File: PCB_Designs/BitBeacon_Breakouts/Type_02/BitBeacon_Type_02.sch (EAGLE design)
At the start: 100 parts, among them IC1 AD8603UJ, IC2 AD8603UJ, IC3 AD8603UJ, IC4 AD8603UJ

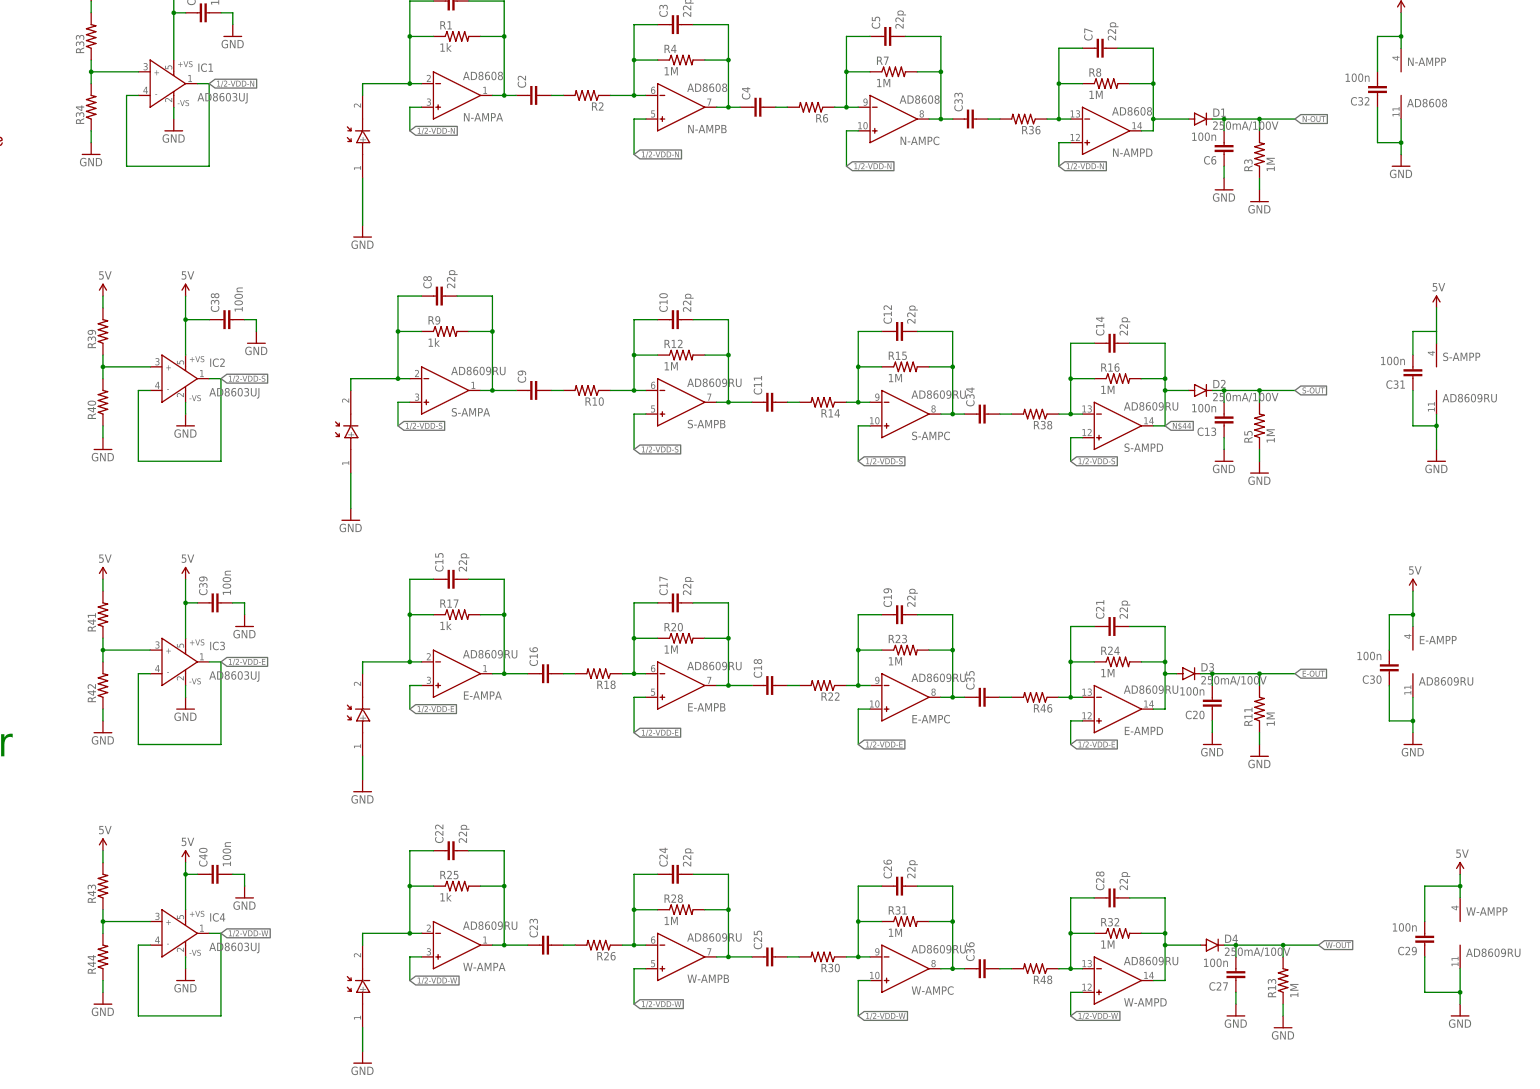
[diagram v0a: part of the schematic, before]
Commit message: updates to code to include Bluetooth, updates to BitBeacon circuit to include labels, indicator LEDs, added BitBeacon Breakout to prototype different signal amplifier types
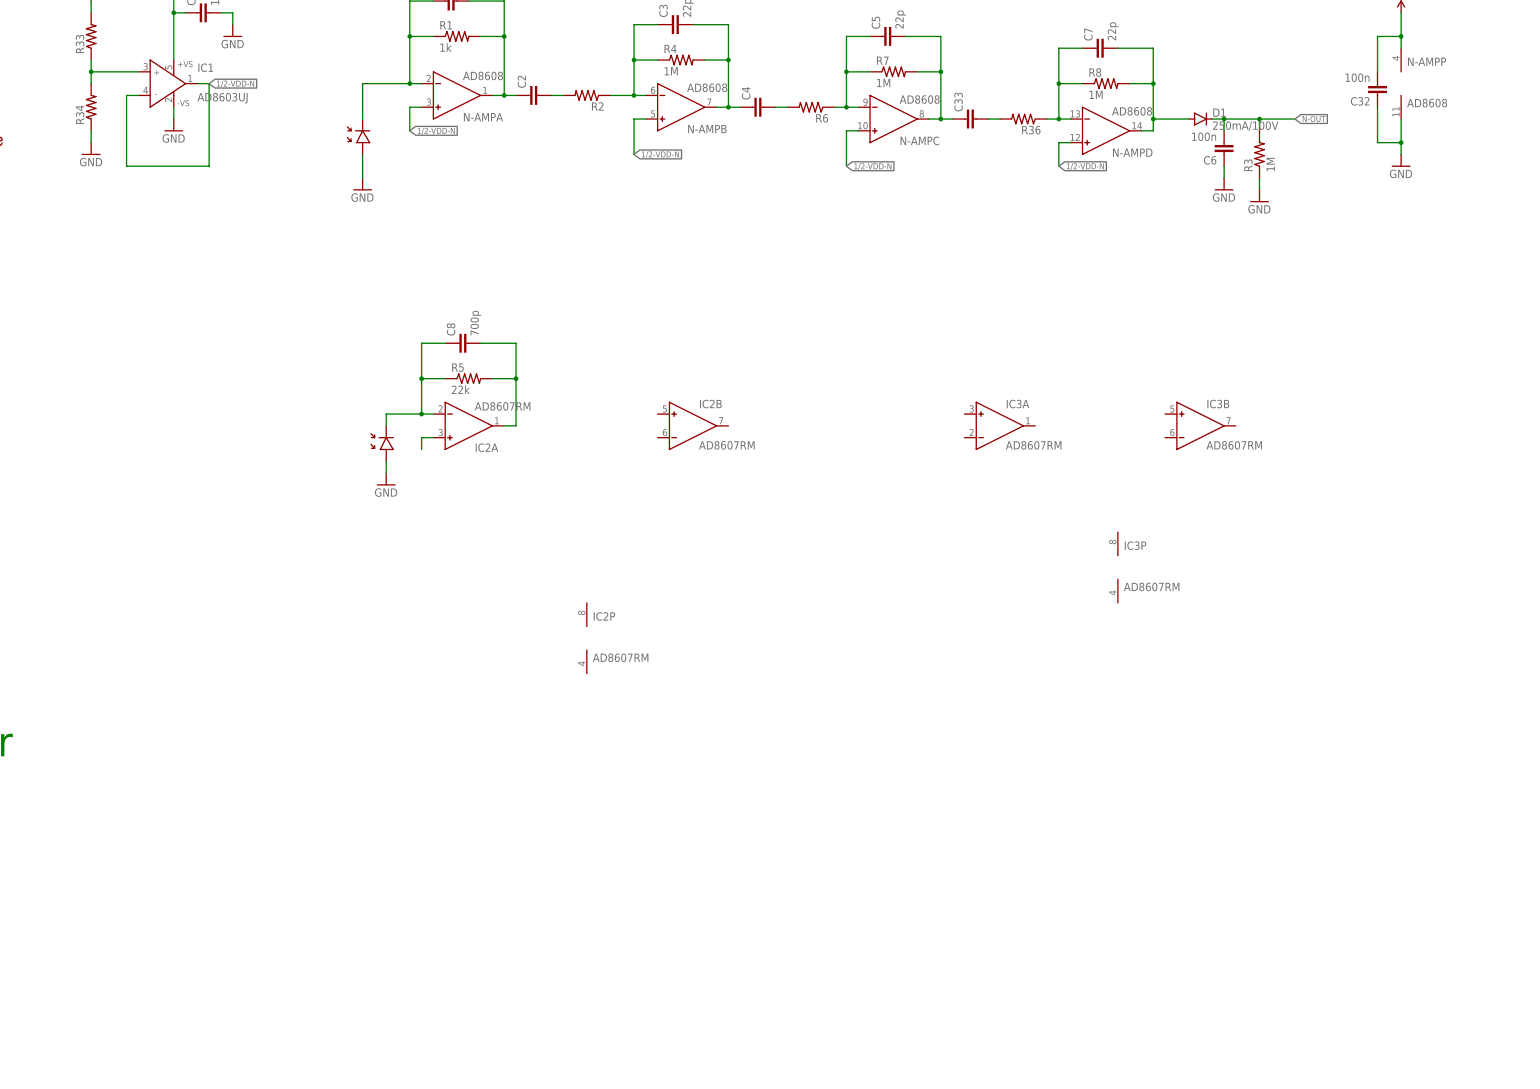
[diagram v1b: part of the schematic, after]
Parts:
- removed C10, C12, C14, C15, C17, C19, C21, C22, C24, C26, C28: 22p, resistor:C-EUC0402
- removed C11, C16, C18, C23, C25, C34, C35, C36, C9: (no value), resistor:C-EUC0402
- removed C13, C20, C27, C29, C30, C31, C38, C39, C40: 100n, resistor:C-EUC0402
- removed D2, D3, D4: 250mA/100V, SparkFun-DiscreteSemi:DIODEBAS16
- removed E-AMP, S-AMP, W-AMP: AD8609RU, analog-devices:AD8609RU
- removed E-PD1, S-PD1, W-PD1: BPW46, Orlando:BPW46
- removed IC4: AD8603UJ, analog-devices:AD8603UJ
- removed R10, R14, R18, R22, R26, R30, R38, R39, R40, R41, R42, R43, R44, R46, R48: (no value), resistor:R-US_R0402
- removed R11, R12, R13, R15, R16, R20, R23, R24, R28, R31, R32: 1M, resistor:R-US_R0402
- removed R17, R25, R9: 1k, resistor:R-US_R0402
- added N-PD2: BPW46, Orlando:BPW46
- C8: value 22p -> 700p
- IC2, IC3: value AD8603UJ -> AD8607RM; device analog-devices:AD8603UJ -> analog-devices:AD8607RM
- R5: value 1M -> 22k
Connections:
- removed net 1/2-VDD-E: E-AMPA.IN+, E-AMPB.IN+, E-AMPC.IN+, E-AMPD.IN+, IC3.IN-, IC3.OUT
- removed net 1/2-VDD-S: IC2.IN-, IC2.OUT, S-AMPA.IN+, S-AMPB.IN+, S-AMPC.IN+, S-AMPD.IN+
- removed net 1/2-VDD-W: IC4.IN-, IC4.OUT, W-AMPA.IN+, W-AMPB.IN+, W-AMPC.IN+, W-AMPD.IN+
- removed net N$12: C10.1, R10.1, R12.1, S-AMPB.IN-
- removed net N$13: C10.2, C11.1, R12.2, S-AMPB.OUT
- removed net N$14: C12.1, R14.1, R15.1, S-AMPC.IN-
- removed net N$15: C12.2, C34.1, R15.2, S-AMPC.OUT
- removed net N$16: IC2.IN+, R39.1, R40.2
- removed net N$17: IC3.IN+, R41.1, R42.2
- removed net N$18: IC4.IN+, R43.1, R44.2
- removed net N$19: C15.1, E-AMPA.IN-, E-PD1.-, R17.1
- removed net N$20: C15.2, C16.1, E-AMPA.OUT, R17.2
- removed net N$21: C17.1, E-AMPB.IN-, R18.1, R20.1
- removed net N$22: C17.2, C18.1, E-AMPB.OUT, R20.2
- removed net N$23: C19.1, E-AMPC.IN-, R22.1, R23.1
- removed net N$24: C19.2, C35.1, E-AMPC.OUT, R23.2
- removed net N$25: C28.1, R32.1, R48.1, W-AMPD.IN-
- removed net N$26: C21.1, E-AMPD.IN-, R24.1, R46.1
- removed net N$28: C22.1, R25.1, W-AMPA.IN-, W-PD1.-
- removed net N$29: C22.2, C23.1, R25.2, W-AMPA.OUT
- removed net N$30: C24.1, R26.1, R28.1, W-AMPB.IN-
- removed net N$31: C24.2, C25.1, R28.2, W-AMPB.OUT
- removed net N$32: C26.1, R30.1, R31.1, W-AMPC.IN-
- removed net N$33: C26.2, C36.1, R31.2, W-AMPC.OUT
- removed net N$36: C34.2, R38.2
- removed net N$37: C11.2, R14.2
- removed net N$38: C9.2, R10.2
- removed net N$39: C35.2, R46.2
- removed net N$40: C18.2, R22.2
- removed net N$41: C16.2, R18.2
- removed net N$42: C36.2, R48.2
- removed net N$43: C25.2, R30.2
- removed net N$44: C14.2, D2.A, R16.2, S-AMPD.OUT
- removed net N$45: C23.2, R26.2
- removed net N$46: C21.2, D3.A, E-AMPD.OUT, R24.2
- removed net N$47: C28.2, D4.A, R32.2, W-AMPD.OUT
- removed net S-AMP: C8.2, C9.1, R9.2, S-AMPA.OUT
- new net VREF: IC2A.IN+
- net 5V: no longer C29.2, C30.2, C31.2, C38.1, C39.1, C40.1, E-AMPP.V+, IC2.+VS, IC3.+VS, IC4.+VS, R39.2, R41.2, R43.2, S-AMPP.V+, W-AMPP.V+
- net E-OUT: no longer C20.2, D3.C, R11.2
- net GND: now also N-PD2.+; no longer C13.1, C20.1, C27.1, C29.1, C30.1, C31.1, C38.2, C39.2, C40.2, E-AMPP.V-, E-PD1.+, IC2.-VS, IC3.-VS, IC4.-VS, R11.1, R13.1, R40.1, R42.1, R44.1, R5.1, S-AMPP.V-, S-PD1.+, W-AMPP.V-, W-PD1.+
- net N$2: now also C8.1, IC2A.IN-, N-PD2.-, R5.1; no longer C14.1, R16.1, R38.1, S-AMPD.IN-
- net N$4: now also C8.2, IC2A.OUT, R5.2; no longer C8.1, R9.1, S-AMPA.IN-, S-PD1.-
- net S-OUT: no longer C13.2, D2.C, R5.2
- net W-OUT: no longer C27.2, D4.C, R13.2
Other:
- moved on the sheet: C8, R5
